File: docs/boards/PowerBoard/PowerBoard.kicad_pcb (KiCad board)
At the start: 2 copper layers, 50 x 100 mm, 3 parts, among them J1 24V IN, J2 5V OUT, U1 URF2405QB-100WR3

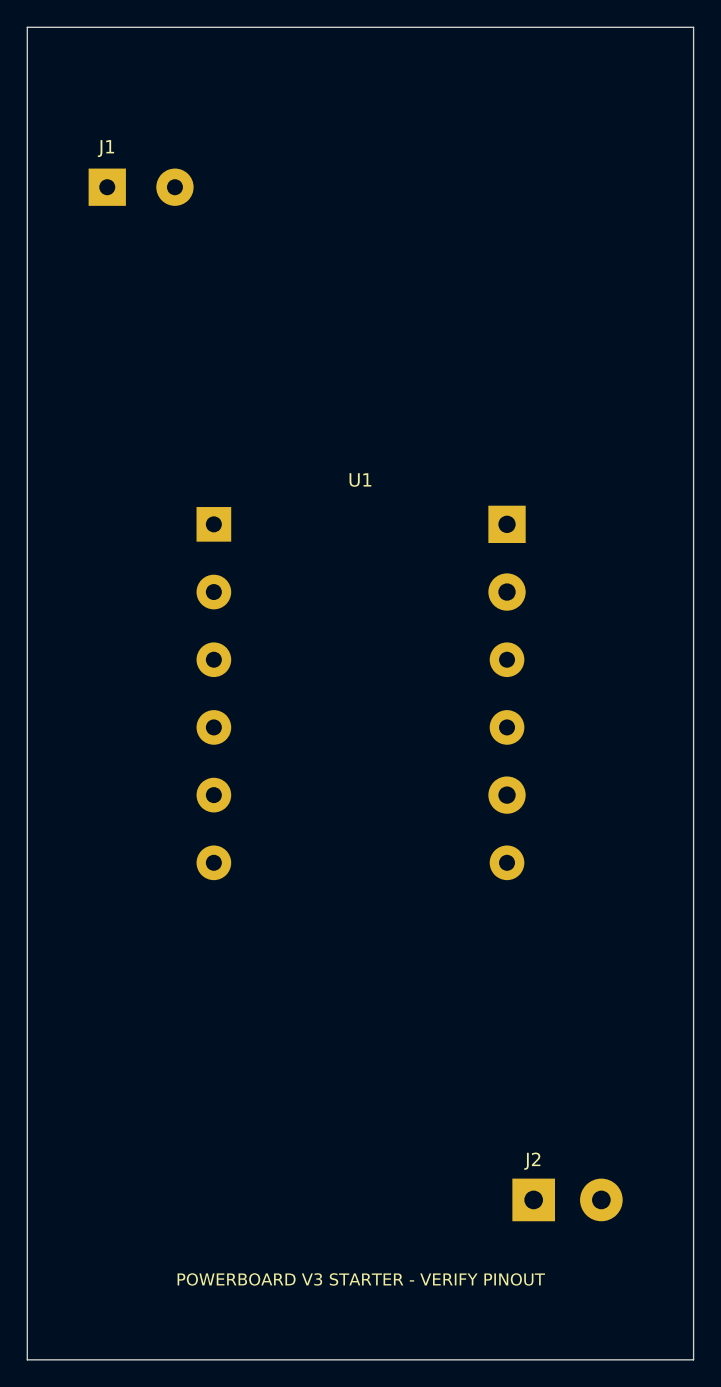
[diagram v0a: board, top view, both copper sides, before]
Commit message: Remake PowerBoard PCB to v4A functional architecture
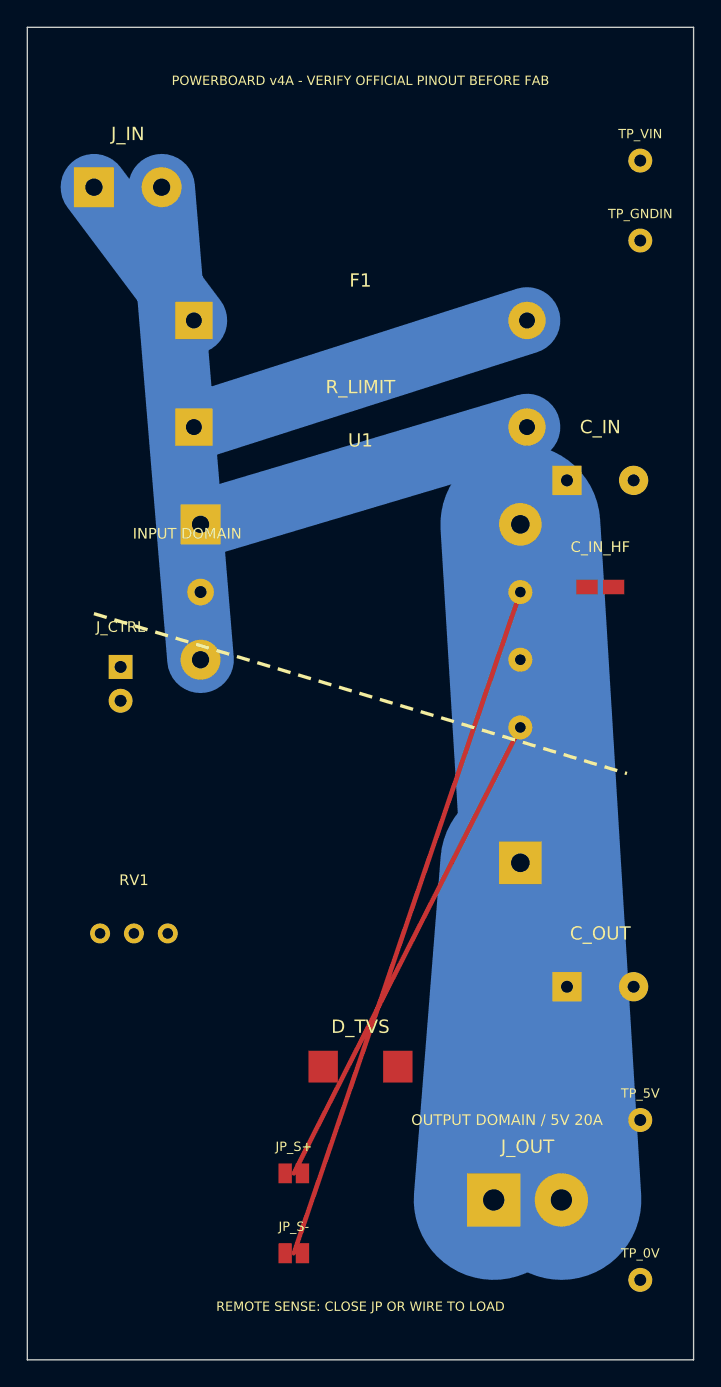
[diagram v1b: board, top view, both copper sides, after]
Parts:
- removed J1: 24V IN, Custom:TerminalBlock_5.08mm_2P
- removed J2: 5V OUT, Custom:TerminalBlock_5.08mm_2P
- added C_IN: 220uF_63V, Custom:CP_D10_P5, F.Cu at (43.0, 34.0)
- added C_IN_HF: 100nF, Custom:C_1206, F.Cu at (43.0, 42.0)
- added C_OUT: 470uF_35V, Custom:CP_D12_P5, F.Cu at (43.0, 72.0)
- added D_TVS: SMDJ7V0A, Custom:TVS_SMC, F.Cu at (25.0, 78.0)
- added F1: 20A_OPTION, Custom:Link_2P_P25, F.Cu at (25.0, 22.0)
- added JP_S+: , Custom:SJ_2P, F.Cu at (20.0, 86.0)
- added JP_S-: , Custom:SJ_2P, F.Cu at (20.0, 92.0)
- added J_CTRL: CTRL_TO_GND_OFF, Custom:Header_1x2, F.Cu at (7.00, 48.0)
- added J_IN: 24V_INPUT, Custom:Terminal_2P_5.08, F.Cu at (5.00, 12.0)
- added J_OUT: 5V_20A_OUT, Custom:Terminal_2P_5.08, F.Cu at (35.0, 88.0)
- added RV1: 10K_TRIM, Custom:Trim_3296W, F.Cu at (8.00, 68.0)
- added R_LIMIT: PRECHARGE, Custom:Power_R_Limit, F.Cu at (25.0, 30.0)
- added TP_0V: , Custom:TP1mm, F.Cu at (46.0, 94.0)
- added TP_5V: , Custom:TP1mm, F.Cu at (46.0, 82.0)
- added TP_GNDIN: , Custom:TP1mm, F.Cu at (46.0, 16.0)
- added TP_VIN: , Custom:TP1mm, F.Cu at (46.0, 10.0)
- U1: footprint Mornsun:URF2405QB-100WR3 -> Custom:URF_QB_100W_VERIFY
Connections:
- U1 pad 1: VIN -> VIN_TO_MODULE
- U1 pad 2: GND_IN -> CTRL
- U1 pad 3: CTRL -> GND_IN
- U1 pad 4: SENSE_N -> OUT_0V
- U1 pad 5: GND_IN -> SENSE_N
- U1 pad 6: SENSE_P -> TRIM
- U1 pad 7: VOUT -> SENSE_P
- U1 pad 8: GND_OUT -> OUT_5V
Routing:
- net SENSE_N: track 0.00 -> 52.5 mm
- net OUT_0V: track 0.00 -> 50.8 mm
- net SENSE_P: track 0.00 -> 37.5 mm
- net GND_IN: track 0.00 -> 35.6 mm
- net VIN_AFTER_F1: track 0.00 -> 26.2 mm
- net VIN_TO_MODULE: track 0.00 -> 25.6 mm
- net OUT_5V: track 0.00 -> 25.4 mm
- net VIN_24V: track 0.00 -> 12.5 mm
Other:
- board text added: "INPUT DOMAIN"
- board text added: "OUTPUT DOMAIN / 5V 20A"
- board text added: "POWERBOARD v4A - VERIFY OFFICIAL PINOUT BEFORE FAB"
- board text added: "REMOTE SENSE: CLOSE JP OR WIRE TO LOAD"
- board text removed: "POWERBOARD V3 STARTER - VERIFY PINOUT"

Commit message: v4C fix PowerBoard URF drills and add required blocks
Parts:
- removed the C_IN at (43.0, 34.0)
- removed the C_IN_HF at (43.0, 42.0)
- removed the C_OUT at (43.0, 72.0)
- removed the D_TVS at (25.0, 78.0)
- removed the JP_S+ at (20.0, 86.0)
- removed the JP_S- at (20.0, 92.0)
- removed the J_CTRL at (7.00, 48.0)
- removed the J_IN at (5.00, 12.0)
- removed the J_OUT at (35.0, 88.0)
- removed the R_LIMIT at (25.0, 30.0)
- removed TP_0V, TP_5V, TP_GNDIN, TP_VIN: , Custom:TP1mm
- added C_IN: 220uF_63V_LOW_ESR, CP_Radial, F.Cu at (43.0, 34.0)
- added C_IN_HF: 10uF_50V, C1206, F.Cu at (43.0, 42.0)
- added C_OUT: 470uF_25V, CP_Radial, F.Cu at (43.0, 72.0)
- added C_OUT_HF: 100nF, C1206, F.Cu at (43.0, 80.0)
- added D_TVS: SELECT_FOR_LOAD_DNP_DEFAULT, TVS_SMC_SELECT, F.Cu at (25.0, 78.0)
- added JP_S+: , Sense_Jumper_Plus, F.Cu at (20.0, 86.0)
- added JP_S-: , Sense_Jumper_Minus, F.Cu at (20.0, 92.0)
- added J_BYP: EXT_RELAY_OR_MOSFET, External_Bypass_Header, F.Cu at (7.00, 32.0)
- added J_CTRL: OPEN_ON_SHORT_OFF, Header_1x2, F.Cu at (7.00, 48.0)
- added J_IN: 24V_IN, Terminal_IN_2P, F.Cu at (5.00, 12.0)
- added J_OUT: 5V_20A_OUT, Terminal_OUT_2P_30A, F.Cu at (35.0, 88.0)
- added R_LIMIT: SIZE_BY_C_BANK, Precharge_R, F.Cu at (25.0, 30.0)
- F1: value 20A_OPTION -> 10A_SLOW_OR_LINK; footprint Custom:Link_2P_P25 -> Fuse_or_Link_10A
- RV1: value 10K_TRIM -> 10K_DNP_UNTIL_TRIM_SET; footprint Custom:Trim_3296W -> Trim_3296W
- U1: footprint Custom:URF_QB_100W_VERIFY -> Mornsun_URF2405QB_100WR3_QB
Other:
- board text added: "POWERBOARD v4C - URF DRILLS FIXED / SENSE MUST BE CLOSED OR WIRED"
- board text removed: "INPUT DOMAIN"
- board text removed: "OUTPUT DOMAIN / 5V 20A"
- board text removed: "POWERBOARD v4A - VERIFY OFFICIAL PINOUT BEFORE FAB"
- board text removed: "REMOTE SENSE: CLOSE JP OR WIRE TO LOAD"

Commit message: v4K add PowerBoard testpoints mounting holes and silkscreen guards
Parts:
- added H1: , MountingHole_M3, F.Cu at (5.00, 5.00)
- added H2: , MountingHole_M3, F.Cu at (45.0, 95.0)
- added TP_0V: , TP1mm, F.Cu at (46.0, 94.0)
- added TP_5V: , TP1mm, F.Cu at (46.0, 82.0)
- added TP_GNDIN: , TP1mm, F.Cu at (46.0, 16.0)
- added TP_S+: , TP1mm, F.Cu at (4.00, 84.0)
- added TP_S-: , TP1mm, F.Cu at (4.00, 90.0)
- added TP_TRIM: , TP1mm, F.Cu at (4.00, 78.0)
- added TP_VIN: , TP1mm, F.Cu at (46.0, 10.0)
- D_TVS: value SELECT_FOR_LOAD_DNP_DEFAULT -> SELECT_DNP_DEFAULT
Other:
- board text added: "INPUT +24V / GND_IN"
- board text added: "OUTPUT +5V / 0V 20A"
- board text added: "POWERBOARD v4K"
- board text added: "PRECHARGE FIRST - BYPASS SECOND"
- board text added: "REMOTE SENSE: CLOSE JP OR WIRE TO LOAD"
- board text removed: "POWERBOARD v4C - URF DRILLS FIXED / SENSE MUST BE CLOSED OR WIRED"
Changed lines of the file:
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@@
   (setup (pad_to_mask_clearance 0.05))
   (net 0 "") (net 1 "VIN_24V") (net 2 "GND_IN") (net 3 "VIN_AFTER_F1") (net 4 "VIN_TO_MODULE") (net 5 "OUT_5V") (net 6 "OUT_0V") (net 7 "CTRL") (net 8 "TRIM") (net 9 "SENSE_P") (net 10 "SENSE_N")
+  (footprint "MountingHole_M3" (layer "F.Cu") (at 5 5)
+    (property "Reference" "H1" (at 0 4 0) (layer "F.SilkS") (effects (font (size 0.7 0.7) (thickness 0.1))))
+    (pad "1" np_thru_hole circle (at 0 0) (size 6.2 6.2) (drill 3.2) (layers "F.Cu" "B.Cu" "F.Mask" "B.Mask"))
+  )
+  (footprint "MountingHole_M3" (layer "F.Cu") (at 45 95)
+    (property "Reference" "H2" (at 0 -4 0) (layer "F.SilkS") (effects (font (size 0.7 0.7) (thickness 0.1))))
+    (pad "1" np_thru_hole circle (at 0 0) (size 6.2 6.2) (drill 3.2) (layers "F.Cu" "B.Cu" "F.Mask" "B.Mask"))
+  )
   (footprint "Terminal_IN_2P" (layer "F.Cu") (at 5 12)
     (property "Reference" "J_IN" (at 2.54 -4 0) (layer "F.SilkS") (effects (font (size 1 1) (thickness 0.15))))
@@
     (fp_line (start 20.1 30.9) (end -20.1 30.9) (stroke (width 0.12) (type default)) (layer "F.SilkS"))
     (fp_line (start -20.1 30.9) (end -20.1 -30.9) (stroke (width 0.12) (type default)) (layer "F.SilkS"))
-    (fp_text user "KEEP COPPER CLEAR UNDER MODULE / VERIFY OFFICIAL PCB LIB" (at 0 0 0) (layer "F.SilkS") (effects (font (size 0.65 0.65) (thickness 0.1))))
+    (fp_text user "NO COPPER UNDER MODULE - VERIFY OFFICIAL FOOTPRINT" (at 0 0 0) (layer "F.SilkS") (effects (font (size 0.65 0.65) (thickness 0.1))))
     (pad "1" thru_hole rect (at -12 -12.7) (size 2.8 2.8) (drill 1.5) (layers "F.Cu" "B.Cu" "F.Mask" "B.Mask") (net 4 "VIN_TO_MODULE"))
     (pad "2" thru_hole oval (at -12 -7.62) (size 2.8 2.8) (drill 1.5) (layers "F.Cu" "B.Cu" "F.Mask" "B.Mask") (net 7 "CTRL"))
@@
   (footprint "TVS_SMC_SELECT" (layer "F.Cu") (at 25 78)
     (property "Reference" "D_TVS" (at 0 -3 0) (layer "F.SilkS") (effects (font (size 0.8 0.8) (thickness 0.12))))
-    (property "Value" "SELECT_FOR_LOAD_DNP_DEFAULT" (at 0 3 0) (layer "F.SilkS") (effects (font (size 0.55 0.55) (thickness 0.08))))
+    (property "Value" "SELECT_DNP_DEFAULT" (at 0 3 0) (layer "F.SilkS") (effects (font (size 0.55 0.55) (thickness 0.08))))
     (pad "1" smd rect (at -2.8 0) (size 2.2 2.4) (layers "F.Cu" "F.Mask") (net 5 "OUT_5V"))
     (pad "2" smd rect (at 2.8 0) (size 2.2 2.4) (layers "F.Cu" "F.Mask") (net 6 "OUT_0V"))
@@
     (pad "2" smd rect (at 0.65 0) (size 1.0 1.5) (layers "F.Cu" "F.Mask") (net 6 "OUT_0V"))
   )
+  (footprint "TP1mm" (layer "F.Cu") (at 46 10) (property "Reference" "TP_VIN" (at 0 -2 0) (layer "F.SilkS") (effects (font (size 0.6 0.6) (thickness 0.08)))) (pad "1" thru_hole circle (at 0 0) (size 1.8 1.8) (drill 0.9) (layers "F.Cu" "B.Cu" "F.Mask" "B.Mask") (net 1 "VIN_24V")))
+  (footprint "TP1mm" (layer "F.Cu") (at 46 16) (property "Reference" "TP_GNDIN" (at 0 -2 0) (layer "F.SilkS") (effects (font (size 0.6 0.6) (thickness 0.08)))) (pad "1" thru_hole circle (at 0 0) (size 1.8 1.8) (drill 0.9) (layers "F.Cu" "B.Cu" "F.Mask" "B.Mask") (net 2 "GND_IN")))
+  (footprint "TP1mm" (layer "F.Cu") (at 46 82) (property "Reference" "TP_5V" (at 0 -2 0) (layer "F.SilkS") (effects (font (size 0.6 0.6) (thickness 0.08)))) (pad "1" thru_hole circle (at 0 0) (size 1.8 1.8) (drill 0.9) (layers "F.Cu" "B.Cu" "F.Mask" "B.Mask") (net 5 "OUT_5V")))
+  (footprint "TP1mm" (layer "F.Cu") (at 46 94) (property "Reference" "TP_0V" (at 0 -2 0) (layer "F.SilkS") (effects (font (size 0.6 0.6) (thickness 0.08)))) (pad "1" thru_hole circle (at 0 0) (size 1.8 1.8) (drill 0.9) (layers "F.Cu" "B.Cu" "F.Mask" "B.Mask") (net 6 "OUT_0V")))
+  (footprint "TP1mm" (layer "F.Cu") (at 4 78) (property "Reference" "TP_TRIM" (at 0 -2 0) (layer "F.SilkS") (effects (font (size 0.6 0.6) (thickness 0.08)))) (pad "1" thru_hole circle (at 0 0) (size 1.8 1.8) (drill 0.9) (layers "F.Cu" "B.Cu" "F.Mask" "B.Mask") (net 8 "TRIM")))
+  (footprint "TP1mm" (layer "F.Cu") (at 4 84) (property "Reference" "TP_S+" (at 0 -2 0) (layer "F.SilkS") (effects (font (size 0.6 0.6) (thickness 0.08)))) (pad "1" thru_hole circle (at 0 0) (size 1.8 1.8) (drill 0.9) (layers "F.Cu" "B.Cu" "F.Mask" "B.Mask") (net 9 "SENSE_P")))
+  (footprint "TP1mm" (layer "F.Cu") (at 4 90) (property "Reference" "TP_S-" (at 0 -2 0) (layer "F.SilkS") (effects (font (size 0.6 0.6) (thickness 0.08)))) (pad "1" thru_hole circle (at 0 0) (size 1.8 1.8) (drill 0.9) (layers "F.Cu" "B.Cu" "F.Mask" "B.Mask") (net 10 "SENSE_N")))
   (segment (start 5 12) (end 12.5 22) (width 5.0) (layer "B.Cu") (net 1))
   (segment (start 37.5 22) (end 12.5 30) (width 5.0) (layer "B.Cu") (net 3))
@@
   (gr_line (start 50 100) (end 0 100) (stroke (width 0.1) (type default)) (layer "Edge.Cuts"))
   (gr_line (start 0 100) (end 0 0) (stroke (width 0.1) (type default)) (layer "Edge.Cuts"))
-  (gr_line (start 5 44) (end 45 56) (stroke (width 0.25) (type dash)) (layer "F.SilkS"))
-  (gr_text "POWERBOARD v4C - URF DRILLS FIXED / SENSE MUST BE CLOSED OR WIRED" (at 25 96 0) (layer "F.SilkS") (effects (font (size 0.62 0.62) (thickness 0.08))))
+  (gr_line (start 4 19) (end 46 19) (stroke (width 0.2) (type dash)) (layer "F.SilkS"))
+  (gr_line (start 4 81) (end 46 81) (stroke (width 0.2) (type dash)) (layer "F.SilkS"))
+  (gr_text "INPUT +24V / GND_IN" (at 17 8 0) (layer "F.SilkS") (effects (font (size 0.75 0.75) (thickness 0.1))))
+  (gr_text "OUTPUT +5V / 0V 20A" (at 34 96 0) (layer "F.SilkS") (effects (font (size 0.75 0.75) (thickness 0.1))))
+  (gr_text "REMOTE SENSE: CLOSE JP OR WIRE TO LOAD" (at 25 92 0) (layer "F.SilkS") (effects (font (size 0.65 0.65) (thickness 0.08))))
+  (gr_text "PRECHARGE FIRST - BYPASS SECOND" (at 24 15 0) (layer "F.SilkS") (effects (font (size 0.65 0.65) (thickness 0.08))))
+  (gr_text "POWERBOARD v4K" (at 25 4 0) (layer "F.SilkS") (effects (font (size 0.75 0.75) (thickness 0.1))))
 )
